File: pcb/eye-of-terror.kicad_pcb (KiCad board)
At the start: 4 copper layers, 200 x 200 mm, 232 parts, among them J1 Conn_01x02_Socket, J2 G-Switch GT-USB-7055E, J3 Conn_01x04, J4 Conn_01x04, J5 Conn_01x03, J6 Conn_01x02_Socket, J7 Conn_01x02_Socket, Q1 IPT020N10N3, Q10 ALS-PT19-315C/L177/TR8, Q11 ALS-PT19-315C/L177/TR8, Q12 ALS-PT19-315C/L177/TR8, Q13 ALS-PT19-315C/L177/TR8, Q14 ALS-PT19-315C/L177/TR8, Q15 ALS-PT19-315C/L177/TR8, Q16 ALS-PT19-315C/L177/TR8, Q17 ALS-PT19-315C/L177/TR8, Q2 IPT020N10N3, Q3 IPT020N10N3, Q4 IPT020N10N3, Q5 IPT020N10N3, Q6 IPT020N10N3, Q7 ALS-PT19-315C/L177/TR8, Q8 ALS-PT19-315C/L177/TR8, Q9 ALS-PT19-315C/L177/TR8, SW1 SW_Push, SW2 SW_Push, U1 RP2350B, U2 TD1660, U3 AP63205WU-7, U4 LSM6DS3, U5 W25Q32JVSS, U7 DRV8353HRTAR, Y1 ABM8-272-T3

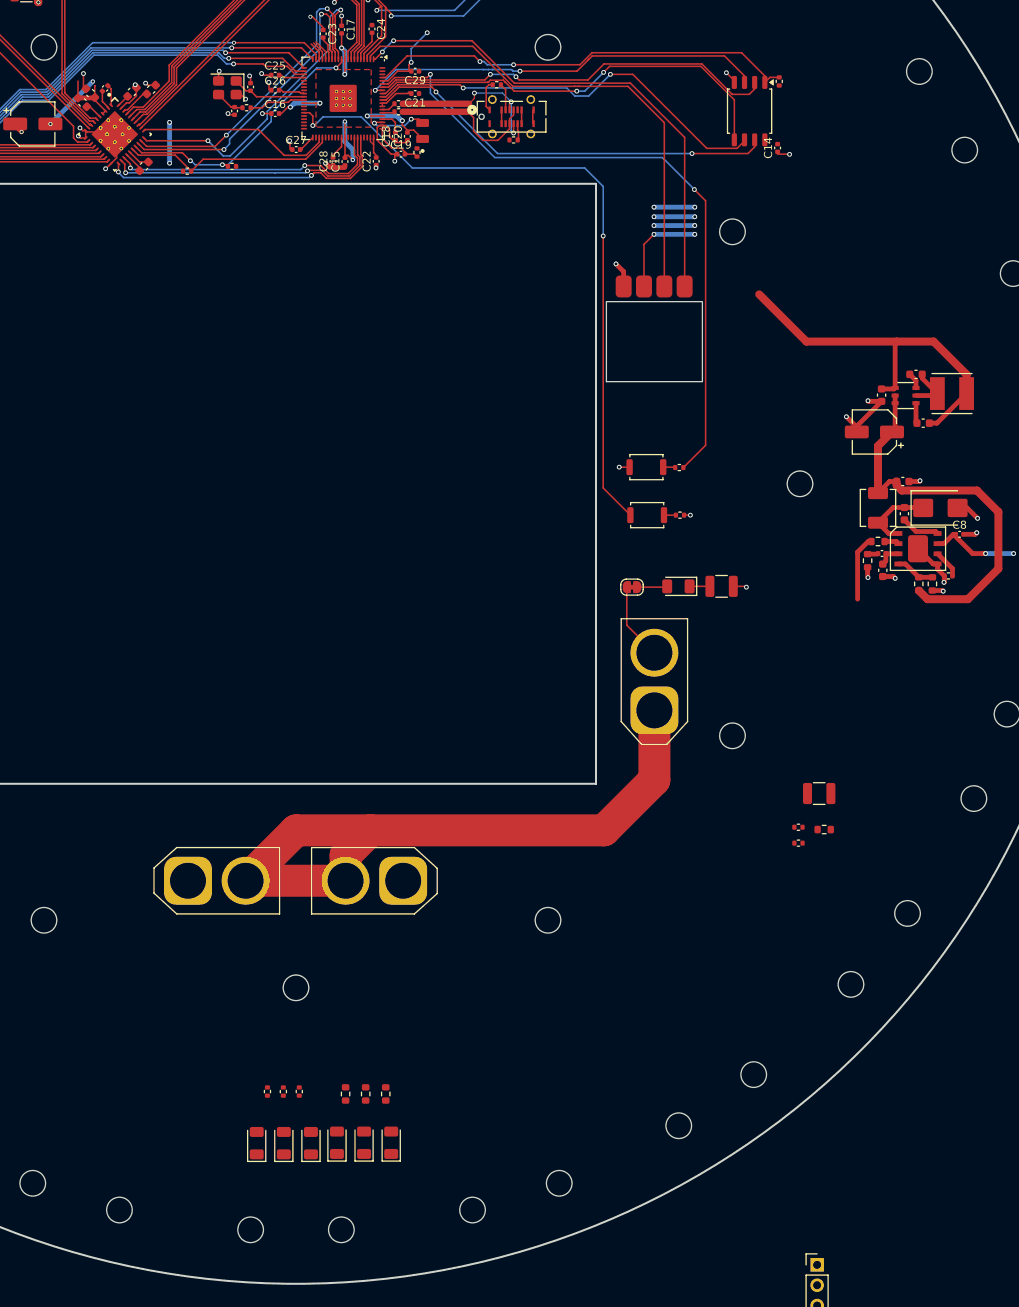
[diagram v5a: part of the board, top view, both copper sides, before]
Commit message: assigned pins to encoder phototransistors
* re-routed some motor driver pins and other stuff
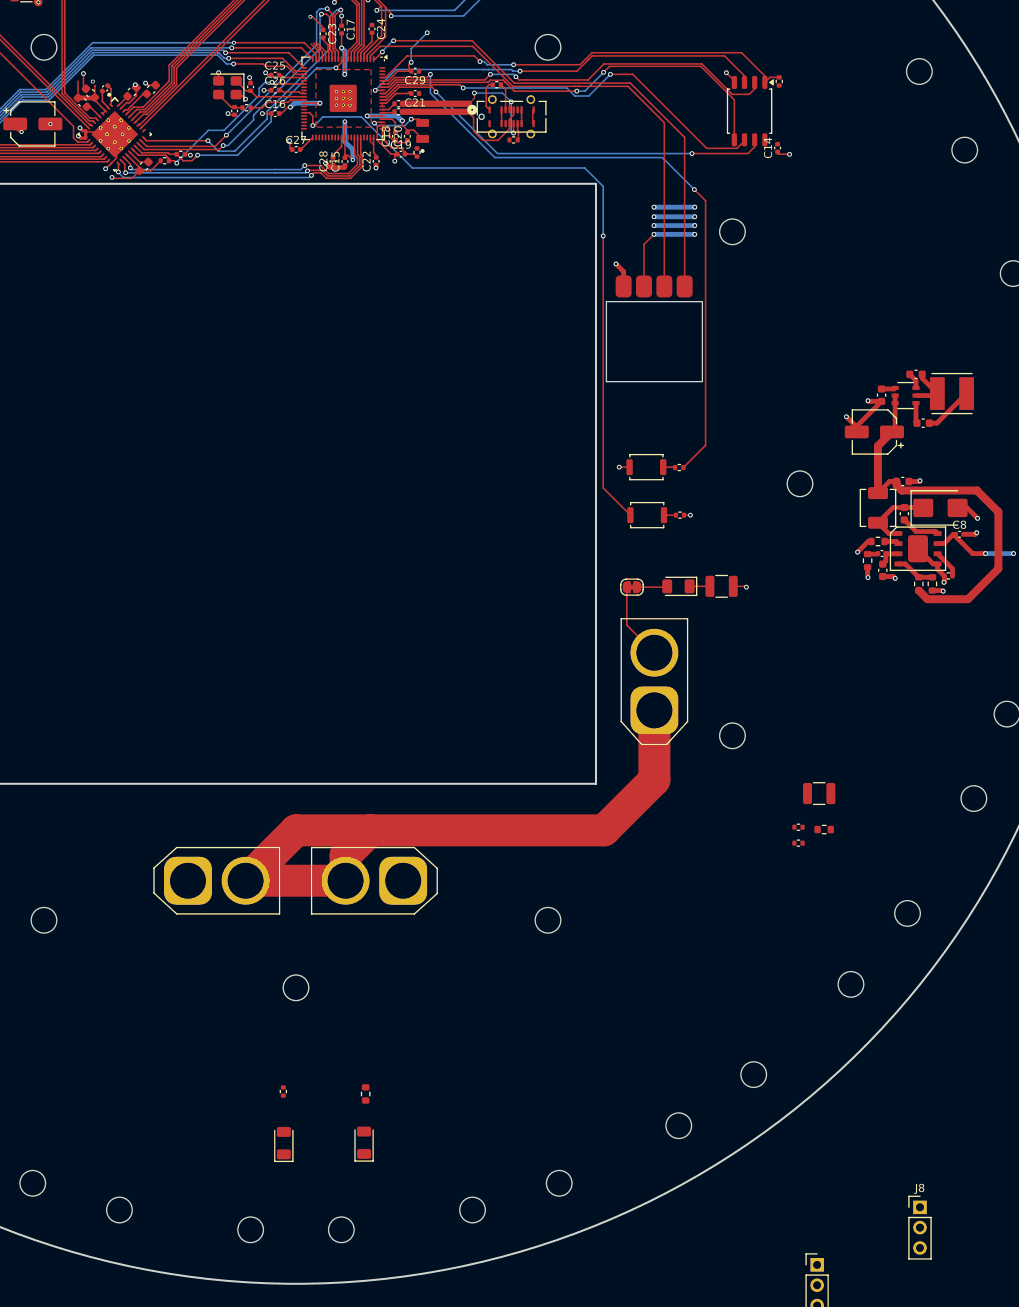
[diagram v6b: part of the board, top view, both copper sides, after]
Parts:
- removed D12, D14: GREEN, Diode_SMD:D_1206_3216Metric
- removed D15, D17: BLUE, Diode_SMD:D_1206_3216Metric
- removed R34, R36: 68, Resistor_SMD:R_0402_1005Metric
- removed R37, R39: 15, Resistor_SMD:R_0603_1608Metric
- added J8: Conn_01x03, Connector_PinHeader_2.54mm:PinHeader_1x03_P2.54mm_Vertical, F.Cu at (386.7, 289.5)
- moved R15 6.57 mm to (294.3, 157.9)
- moved R16 3.09 mm to (292.3, 158.7)
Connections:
- U1 pad 25: unconnected-(U1-GPIO24-Pad25) -> /DRIVER_ENABLE
- U1 pad 26: unconnected-(U1-GPIO25-Pad26) -> /DRIVER_FAULTn
- U1 pad 36: /GREEN_LED_0 -> /ENC_SENSE_1
- U1 pad 37: /GREEN_LED_1 -> /ENC_SENSE_2
- U1 pad 38: /GREEN_LED_2 -> /ENC_SENSE_3
- U1 pad 39: /BLUE_LED_0 -> /ENC_SENSE_4
- U1 pad 40: /BLUE_LED_1 -> /ENC_SENSE_5
- U1 pad 42: /BLUE_LED_2 -> /ENC_SENSE_6
- U1 pad 43: /DRIVER_ENABLE -> /ENC_SENSE_7
- U1 pad 44: /DRIVER_FAULTn -> /ENC_SENSE_8
- U1 pad 45: unconnected-(U1-GPIO36-Pad45) -> /ENC_SENSE_9
- U1 pad 46: unconnected-(U1-GPIO37-Pad46) -> /ENC_SENSE_10
- U1 pad 47: unconnected-(U1-GPIO38-Pad47) -> /ENC_SENSE_11
- U1 pad 78: unconnected-(U1-GPIO1-Pad78) -> /GREEN_LED_1
- U1 pad 79: unconnected-(U1-GPIO2-Pad79) -> /BLUE_LED_1
- U1 pad 80: unconnected-(U1-GPIO3-Pad80) -> /GPIO3
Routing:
- net +3V3: track 118.5 -> 82.8 mm
- net /DRIVER_ENABLE: track 24.6 -> 0.00 mm
- net +BATT: track 55.9 -> 42.6 mm, vias 4 -> 5
- net /DRIVER_CIPO: track 33.9 -> 32.6 mm, vias 3 -> 2
- net DGND: track 46.2 -> 44.9 mm
- net /DRIVER_FAULTn: track 27.0 -> 27.2 mm, vias 0 -> 2
- added copper zone on In1.Cu, net +BATT
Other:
- board text removed: "For Instructional Use Only."
- board text removed: "SOLIDWORKS Educational Product."

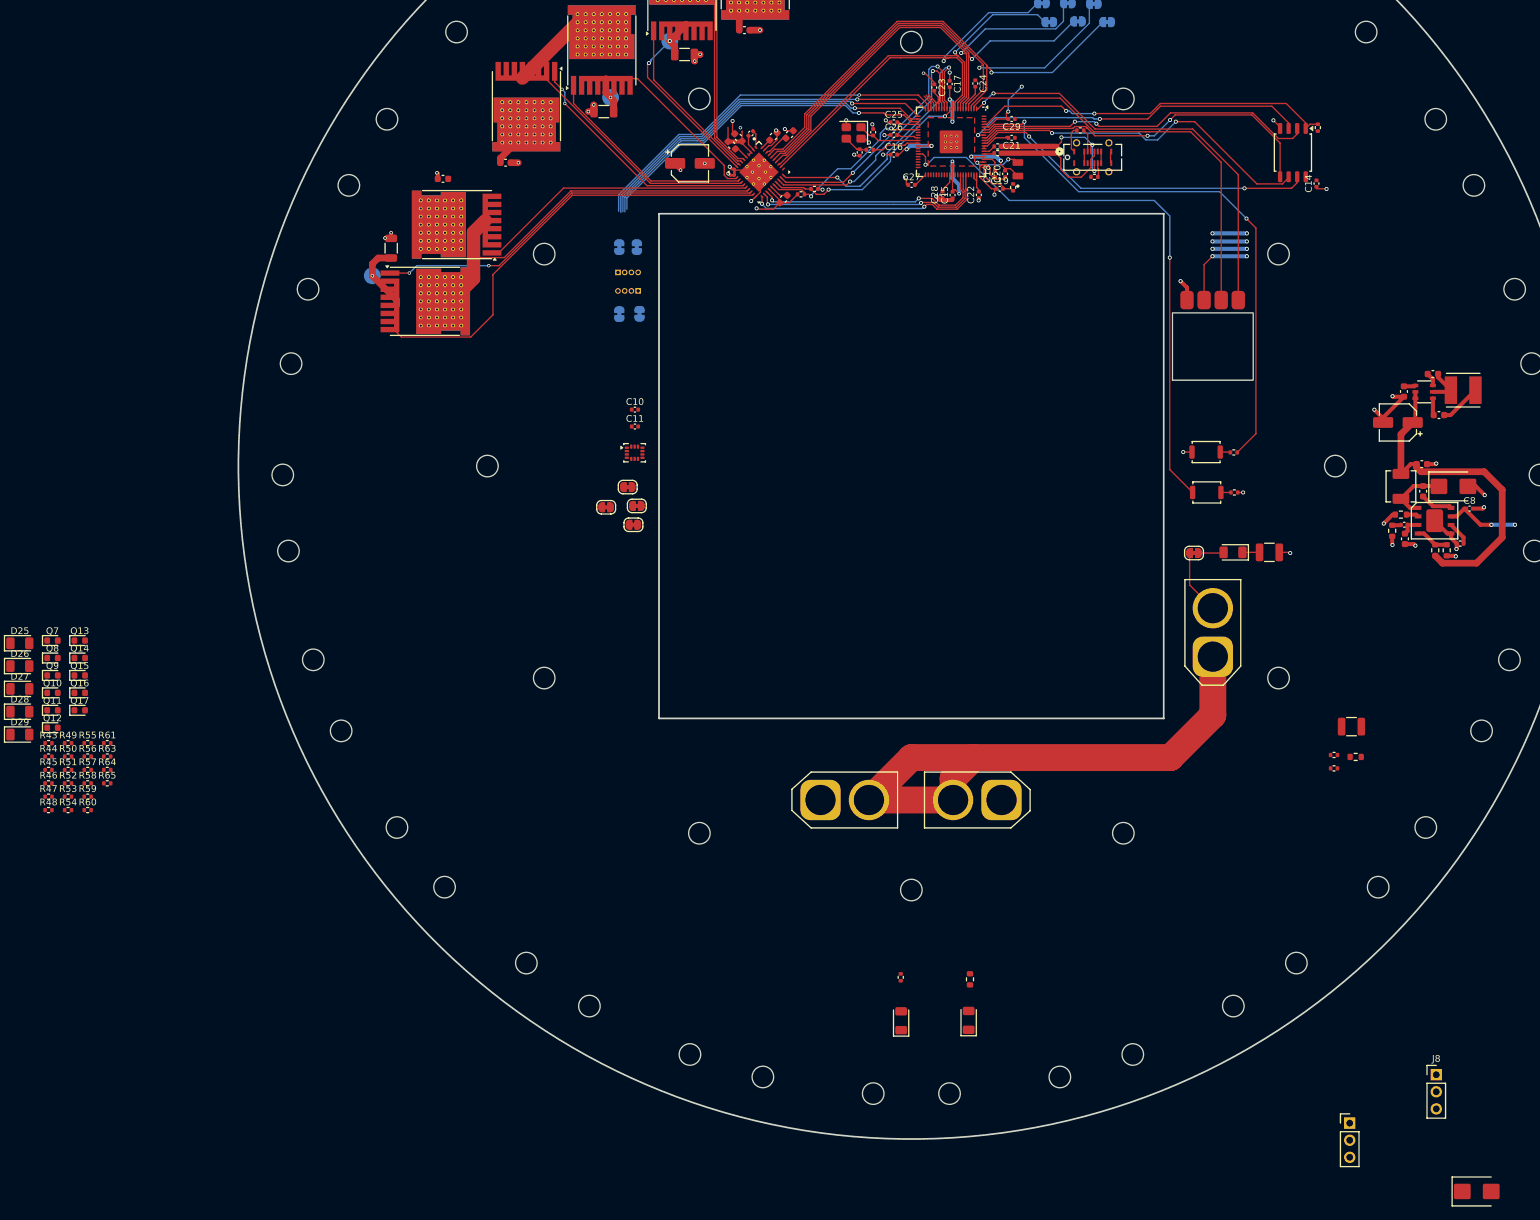
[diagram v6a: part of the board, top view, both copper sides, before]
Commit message: added BATT and PGND power planes for motor drivers
started adding traces for phototransistors
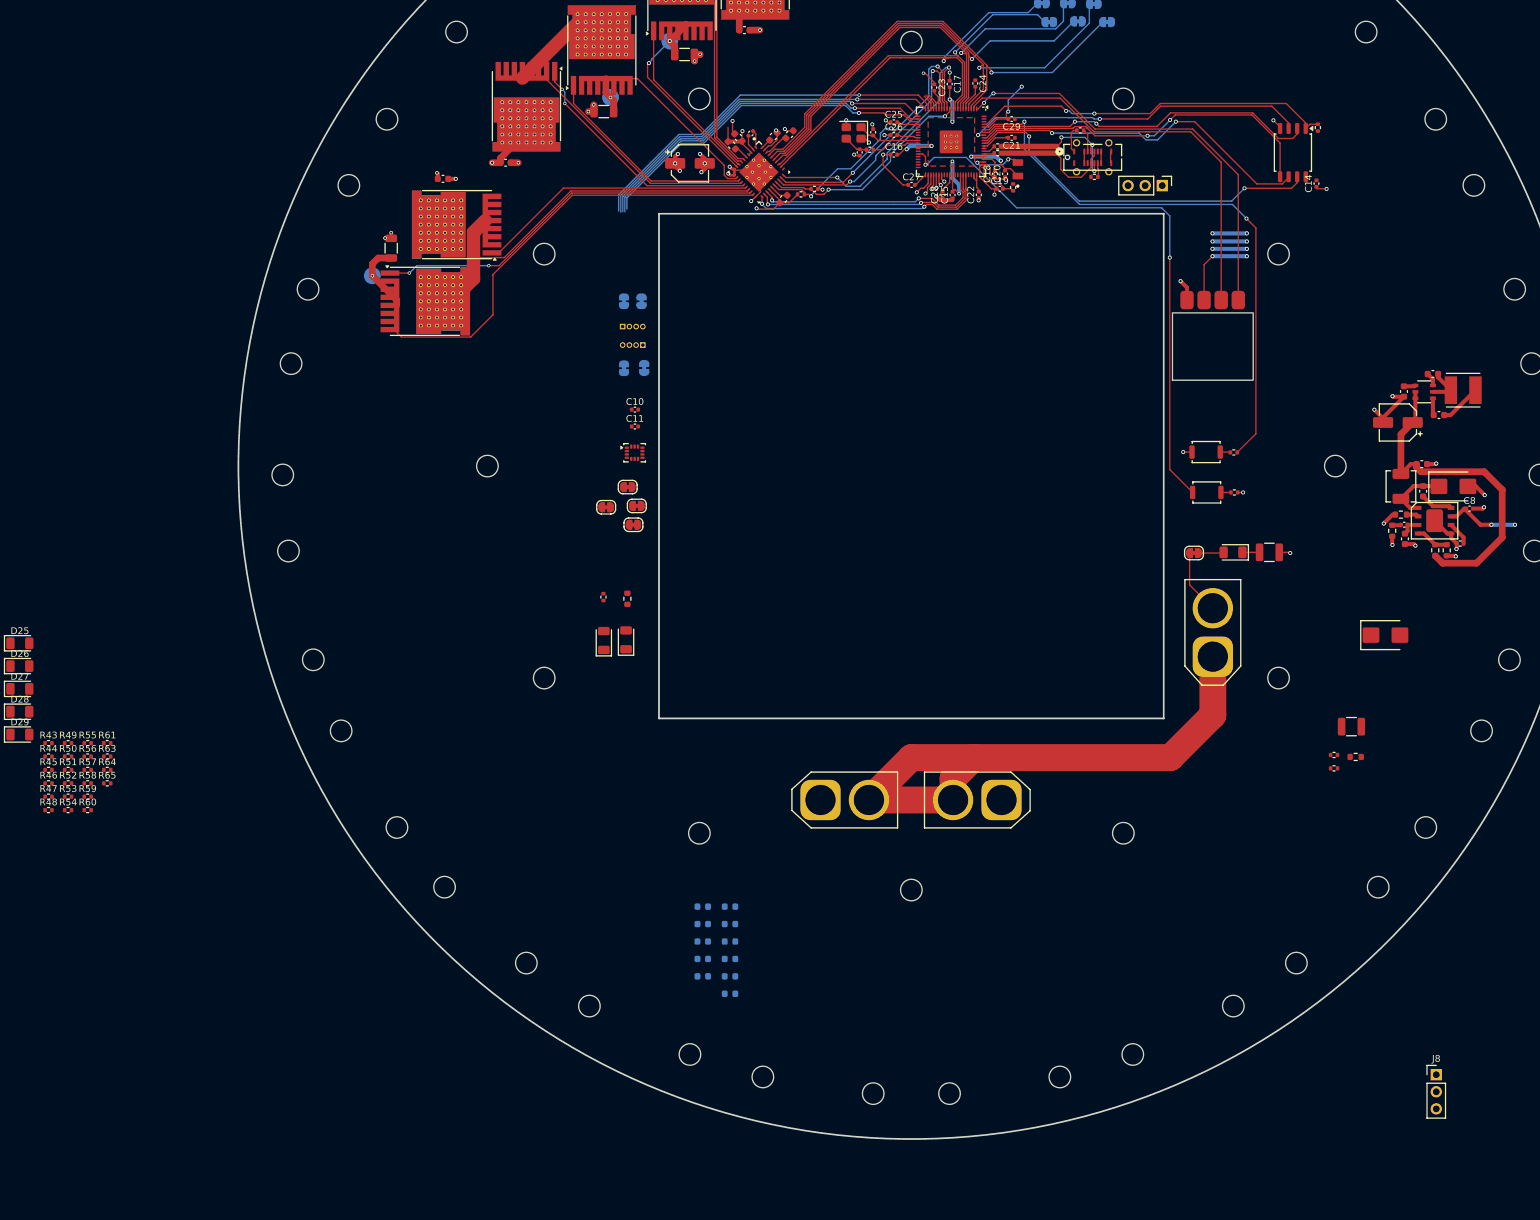
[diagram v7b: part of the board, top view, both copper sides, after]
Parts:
- Q10, Q11, Q12, Q13, Q14, Q15, Q16, Q17, Q7, Q8, Q9: moved to B.Cu
- moved J5 142.1 mm to (346.0, 157.4), turned to -90 degrees
- moved Q11 108.2 mm to (281.8, 274.9), turned to 180 degrees
- moved Q7 108.2 mm to (281.8, 264.6), turned to 180 degrees
- moved Q9 108.2 mm to (281.8, 269.7), turned to 180 degrees
- moved Q10 108.2 mm to (281.8, 272.3), turned to 180 degrees
- moved Q12 108.2 mm to (281.8, 277.5), turned to 180 degrees
- moved Q8 108.2 mm to (281.8, 267.1), turned to 180 degrees
- moved Q13 100.7 mm to (277.7, 264.6), turned to 180 degrees
- moved Q14 100.7 mm to (277.7, 267.1), turned to 180 degrees
- moved Q15 100.7 mm to (277.7, 269.7), turned to 180 degrees
- moved Q16 100.7 mm to (277.7, 272.3), turned to 180 degrees
- moved Q17 100.7 mm to (277.7, 274.9), turned to 180 degrees
- moved D1 83.8 mm to (379.1, 224.2)
- moved R38 76.1 mm to (266.5, 218.8)
- moved D16 76.1 mm to (266.3, 224.9)
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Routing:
- net +BATT: track 42.6 -> 48.1 mm, vias 5 -> 9
- net DGND: track 44.9 -> 50.4 mm, vias 21 -> 20
- net /ENC_SENSE_6: track 0.00 -> 3.54 mm, vias 0 -> 1
- net /ENC_SENSE_7: track 0.00 -> 3.13 mm, vias 0 -> 1
- net /QSPI_SD3: track 51.9 -> 54.8 mm
- net /ENC_SENSE_8: track 0.00 -> 2.24 mm, vias 0 -> 1
- net /ENC_SENSE_9: track 0.00 -> 1.96 mm, vias 0 -> 1
- net PGND: track 52.7 -> 54.5 mm, vias 23 -> 25
- net /ENC_SENSE_10: track 0.00 -> 1.65 mm, vias 0 -> 1
- net /ENC_SENSE_11: track 0.00 -> 1.17 mm, vias 0 -> 1
- net /QSPI_SS: track 83.3 -> 84.3 mm
- added copper zone on In2.Cu, net PGND
